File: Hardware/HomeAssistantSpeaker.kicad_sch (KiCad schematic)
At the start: 29 parts, among them J1 USB_C_Receptacle_USB2.0, J2 Speaker, J3 Prog, J4 LED, U1 ESP32-WROOM-32, U2 LM1117-3.3, U3 MAX98357AETE+

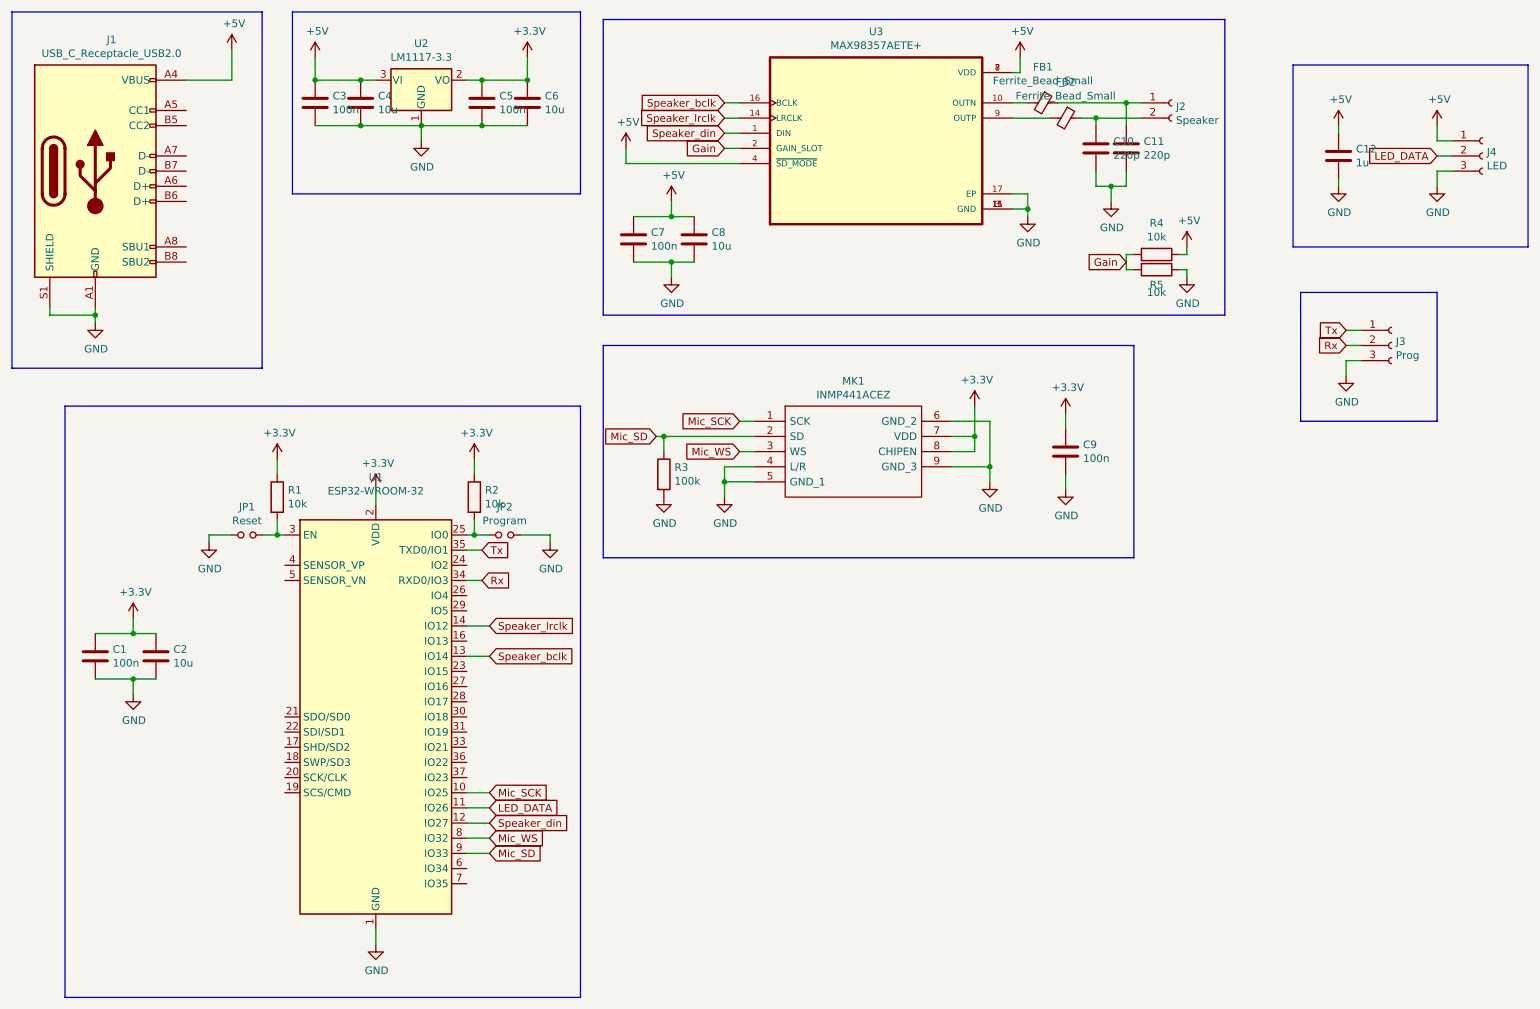
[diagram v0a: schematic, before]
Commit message: Rev B:
* Added missing resitiors for usb c power
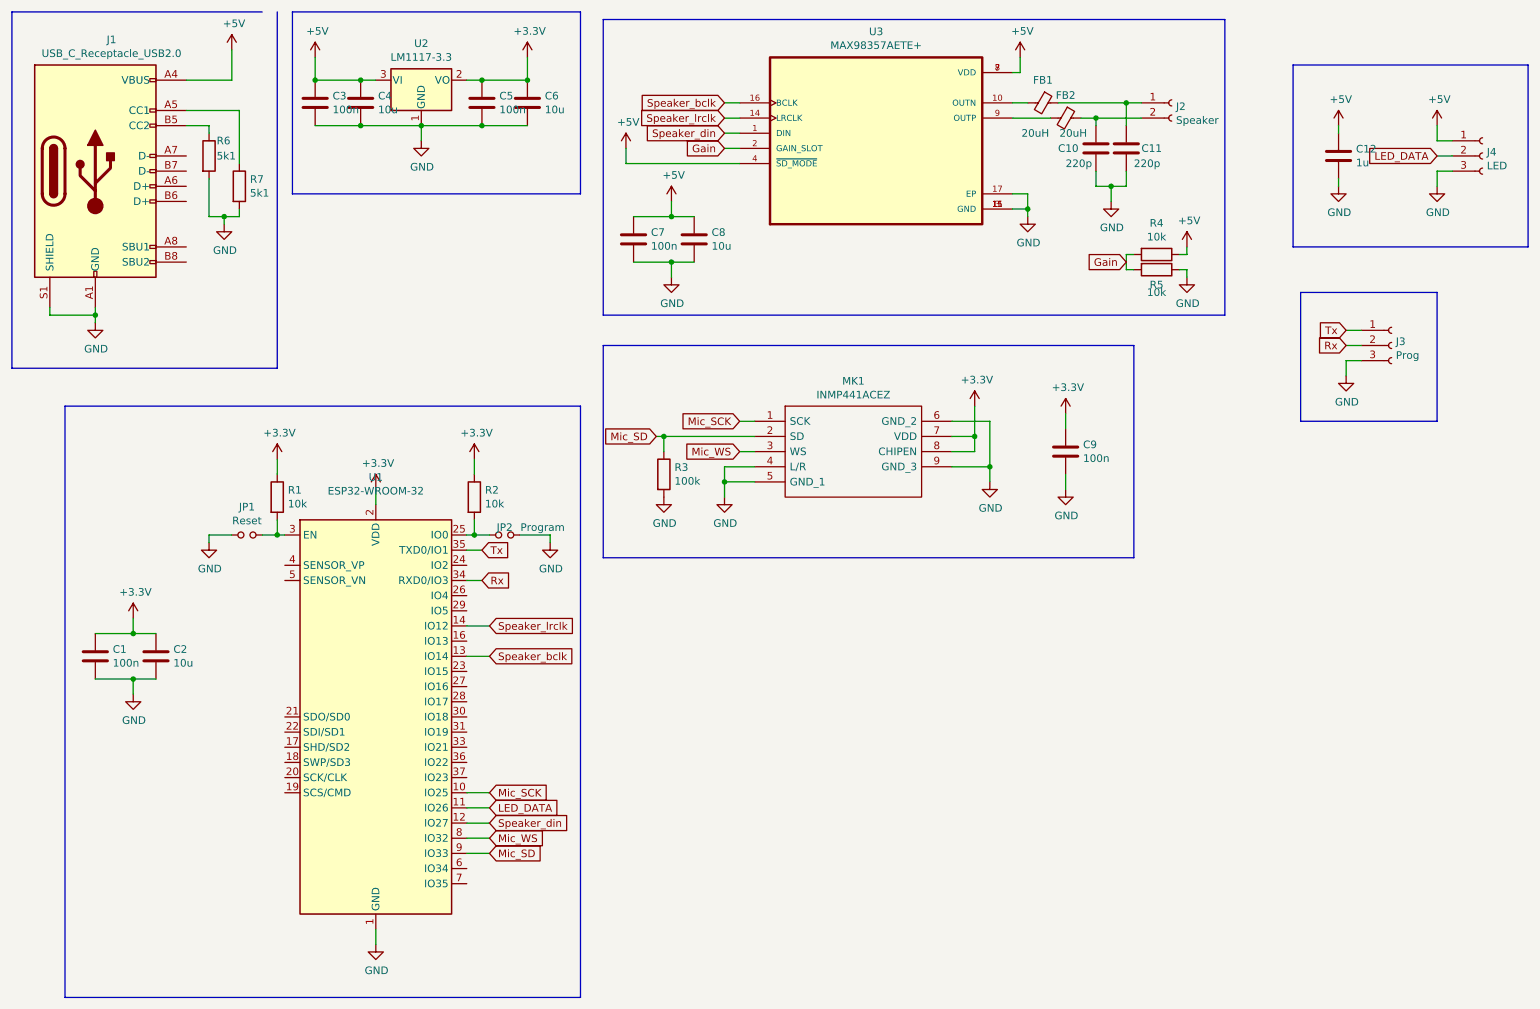
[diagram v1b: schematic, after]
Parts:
- added R6, R7: 5k1, Resistor_SMD:R_0805_2012Metric, symbol Device:R
- FB1, FB2: value Ferrite_Bead_Small -> 20uH
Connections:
- net GND: now also R6.2, R7.2
- net at J1.A5 (CC1): now also R7.1
- net at J1.B5 (CC2): now also R6.1
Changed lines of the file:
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@@
   (title_block
     (title "HomeAssistantSpeaker")
-    (date "2022-11-20")
-    (rev "A")
+    (date "2022-12-29")
+    (rev "B")
     (company "Paweł Warzecha")
   )
@@
   (junction (at 102.87 25.4) (diameter 0) (color 0 0 0 0)
   )
+  (junction (at 52.07 48.26) (diameter 0) (color 0 0 0 0)
+  )
   (junction (at 127 55.88) (diameter 0) (color 0 0 0 0)
   )
@@
     (stroke (width 0) (type default) (color 0 0 0 0))
   )
+  (wire (pts (xy 54.61 30.48) (xy 54.61 39.37))
+    (stroke (width 0) (type default) (color 0 0 0 0))
+  )
   (wire (pts (xy 184.15 46.99) (xy 186.69 46.99))
     (stroke (width 0) (type default) (color 0 0 0 0))
@@
     (stroke (width 0) (type default) (color 0 0 0 0))
   )
+  (wire (pts (xy 49.53 33.02) (xy 49.53 34.29))
+    (stroke (width 0) (type default) (color 0 0 0 0))
+  )
   (wire (pts (xy 96.52 149.86) (xy 92.71 149.86))
     (stroke (width 0) (type default) (color 0 0 0 0))
@@
     (stroke (width 0) (type default) (color 0 0 0 0))
   )
+  (wire (pts (xy 54.61 46.99) (xy 54.61 48.26))
+    (stroke (width 0) (type default) (color 0 0 0 0))
+  )
   (wire (pts (xy 92.71 104.14) (xy 95.25 104.14))
     (stroke (width 0) (type default) (color 0 0 0 0))
@@
     (stroke (width 0) (type default) (color 0 0 0 0))
   )
+  (wire (pts (xy 52.07 48.26) (xy 52.07 49.53))
+    (stroke (width 0) (type default) (color 0 0 0 0))
+  )
   (polyline (pts (xy 204.47 69.85) (xy 115.57 69.85))
     (stroke (width 0) (type default) (color 0 0 0 0))
@@
     (stroke (width 0) (type default) (color 0 0 0 0))
   )
+  (wire (pts (xy 45.72 33.02) (xy 49.53 33.02))
+    (stroke (width 0) (type default) (color 0 0 0 0))
+  )
   (wire (pts (xy 93.98 91.44) (xy 93.98 88.9))
     (stroke (width 0) (type default) (color 0 0 0 0))
@@
     (stroke (width 0) (type default) (color 0 0 0 0))
   )
+  (wire (pts (xy 45.72 30.48) (xy 54.61 30.48))
+    (stroke (width 0) (type default) (color 0 0 0 0))
+  )
   (polyline (pts (xy 255.27 82.55) (xy 232.41 82.55))
     (stroke (width 0) (type default) (color 0 0 0 0))
@@
     (stroke (width 0) (type default) (color 0 0 0 0))
   )
-  (polyline (pts (xy 58.42 73.66) (xy 16.51 73.66))
+  (polyline (pts (xy 60.96 73.66) (xy 16.51 73.66))
+    (stroke (width 0) (type default) (color 0 0 0 0))
+  )
+  (wire (pts (xy 49.53 48.26) (xy 52.07 48.26))
     (stroke (width 0) (type default) (color 0 0 0 0))
   )
@@
     (stroke (width 0) (type default) (color 0 0 0 0))
   )
+  (wire (pts (xy 52.07 48.26) (xy 54.61 48.26))
+    (stroke (width 0) (type default) (color 0 0 0 0))
+  )
   (polyline (pts (xy 63.5 44.45) (xy 63.5 13.97))
     (stroke (width 0) (type default) (color 0 0 0 0))
@@
     (stroke (width 0) (type default) (color 0 0 0 0))
   )
+  (wire (pts (xy 49.53 41.91) (xy 49.53 48.26))
+    (stroke (width 0) (type default) (color 0 0 0 0))
+  )
   (wire (pts (xy 53.34 101.6) (xy 49.53 101.6))
     (stroke (width 0) (type default) (color 0 0 0 0))
@@
     (stroke (width 0) (type default) (color 0 0 0 0))
   )
-  (polyline (pts (xy 58.42 13.97) (xy 58.42 73.66))
+  (polyline (pts (xy 60.96 13.97) (xy 60.96 73.66))
     (stroke (width 0) (type default) (color 0 0 0 0))
   )
@@
   (symbol (lib_id "HomeAssistantSpeaker-rescue:Jumper_NO_Small-Device") (at 99.06 101.6 0) (unit 1)
     (in_bom yes) (on_board yes)
-    (property "Reference" "JP2" (id 0) (at 99.06 96.901 0))
-    (property "Value" "Program" (id 1) (at 99.06 99.2124 0))
+    (property "Reference" "JP2" (id 0) (at 99.06 100.33 0))
+    (property "Value" "Program" (id 1) (at 105.41 100.33 0))
     (property "Footprint" "Jumper:SolderJumper-2_P1.3mm_Open_RoundedPad1.0x1.5mm" (id 2) (at 99.06 101.6 0)
       (effects (font (size 1.27 1.27)) hide)
@@
   (symbol (lib_id "HomeAssistantSpeaker-rescue:Ferrite_Bead_Small-Device") (at 189.23 29.21 270) (unit 1)
     (in_bom yes) (on_board yes)
-    (property "Reference" "FB1" (id 0) (at 189.23 23.1902 90))
-    (property "Value" "Ferrite_Bead_Small" (id 1) (at 189.23 25.5016 90))
+    (property "Reference" "FB1" (id 0) (at 189.23 25.4 90))
+    (property "Value" "20uH" (id 1) (at 187.96 34.29 90))
     (property "Footprint" "Inductor_SMD:L_0805_2012Metric" (id 2) (at 189.23 27.432 90)
       (effects (font (size 1.27 1.27)) hide)
@@
   (symbol (lib_id "HomeAssistantSpeaker-rescue:Ferrite_Bead_Small-Device") (at 193.04 31.75 270) (unit 1)
     (in_bom yes) (on_board yes)
-    (property "Reference" "FB2" (id 0) (at 193.04 25.7302 90))
-    (property "Value" "Ferrite_Bead_Small" (id 1) (at 193.04 28.0416 90))
+    (property "Reference" "FB2" (id 0) (at 193.04 27.94 90))
+    (property "Value" "20uH" (id 1) (at 194.31 34.29 90))
     (property "Footprint" "Inductor_SMD:L_0805_2012Metric" (id 2) (at 193.04 29.972 90)
       (effects (font (size 1.27 1.27)) hide)
@@
   (symbol (lib_id "Device:C") (at 203.2 36.83 0) (unit 1)
     (in_bom yes) (on_board yes)
-    (property "Reference" "C11" (id 0) (at 206.121 35.6616 0)
-      (effects (font (size 1.27 1.27)) (justify left))
-    )
-    (property "Value" "220p" (id 1) (at 206.121 37.973 0)
+    (property "Reference" "C11" (id 0) (at 205.74 36.83 0)
+      (effects (font (size 1.27 1.27)) (justify left))
+    )
+    (property "Value" "220p" (id 1) (at 204.47 39.37 0)
       (effects (font (size 1.27 1.27)) (justify left))
     )
@@
   (symbol (lib_id "Device:C") (at 198.12 36.83 0) (unit 1)
     (in_bom yes) (on_board yes)
-    (property "Reference" "C10" (id 0) (at 201.041 35.6616 0)
-      (effects (font (size 1.27 1.27)) (justify left))
-    )
-    (property "Value" "220p" (id 1) (at 201.041 37.973 0)
+    (property "Reference" "C10" (id 0) (at 191.77 36.83 0)
+      (effects (font (size 1.27 1.27)) (justify left))
+    )
+    (property "Value" "220p" (id 1) (at 193.04 39.37 0)
       (effects (font (size 1.27 1.27)) (justify left))
     )
@@
     (pin "1")
   )
+  (symbol (lib_id "Device:R") (at 54.61 43.18 0) (unit 1)
+    (in_bom yes) (on_board yes)
+    (property "Reference" "R7" (id 0) (at 56.388 42.0116 0)
+      (effects (font (size 1.27 1.27)) (justify left))
+    )
+    (property "Value" "5k1" (id 1) (at 56.388 44.323 0)
+      (effects (font (size 1.27 1.27)) (justify left))
+    )
+    (property "Footprint" "Resistor_SMD:R_0805_2012Metric" (id 2) (at 52.832 43.18 90)
+      (effects (font (size 1.27 1.27)) hide)
+    )
+    (property "Datasheet" "~" (id 3) (at 54.61 43.18 0)
+      (effects (font (size 1.27 1.27)) hide)
+    )
+    (pin "1")
+    (pin "2")
+  )
+  (symbol (lib_id "Device:R") (at 49.53 38.1 0) (unit 1)
+    (in_bom yes) (on_board yes)
+    (property "Reference" "R6" (id 0) (at 50.8 35.56 0)
+      (effects (font (size 1.27 1.27)) (justify left))
+    )
+    (property "Value" "5k1" (id 1) (at 50.8 38.1 0)
+      (effects (font (size 1.27 1.27)) (justify left))
+    )
+    (property "Footprint" "Resistor_SMD:R_0805_2012Metric" (id 2) (at 47.752 38.1 90)
+      (effects (font (size 1.27 1.27)) hide)
+    )
+    (property "Datasheet" "~" (id 3) (at 49.53 38.1 0)
+      (effects (font (size 1.27 1.27)) hide)
+    )
+    (pin "1")
+    (pin "2")
+  )
+  (symbol (lib_id "power:GND") (at 52.07 49.53 0) (unit 1)
+    (in_bom yes) (on_board yes)
+    (property "Reference" "#PWR01" (id 0) (at 52.07 55.88 0)
+      (effects (font (size 1.27 1.27)) hide)
+    )
+    (property "Value" "GND" (id 1) (at 52.197 53.9242 0))
+    (property "Footprint" "" (id 2) (at 52.07 49.53 0)
+      (effects (font (size 1.27 1.27)) hide)
+    )
+    (property "Datasheet" "" (id 3) (at 52.07 49.53 0)
+      (effects (font (size 1.27 1.27)) hide)
+    )
+    (pin "1")
+  )
   (sheet_instances
     (path "/" (page "1"))
   )
   (symbol_instances
+    (path "/c957bf7f-3e92-4741-b985-0817aefda6cb"
+      (reference "#PWR01") (unit 1) (value "GND") (footprint "")
+    )
     (path "/00000000-0000-0000-0000-000062f94a7c"
       (reference "#PWR0101") (unit 1) (value "+5V") (footprint "")
@@
     )
     (path "/00000000-0000-0000-0000-0000637db72b"
-      (reference "FB1") (unit 1) (value "Ferrite_Bead_Small") (footprint "Inductor_SMD:L_0805_2012Metric")
+      (reference "FB1") (unit 1) (value "20uH") (footprint "Inductor_SMD:L_0805_2012Metric")
     )
     (path "/00000000-0000-0000-0000-0000637dc15d"
-      (reference "FB2") (unit 1) (value "Ferrite_Bead_Small") (footprint "Inductor_SMD:L_0805_2012Metric")
+      (reference "FB2") (unit 1) (value "20uH") (footprint "Inductor_SMD:L_0805_2012Metric")
     )
     (path "/00000000-0000-0000-0000-000062f890e9"
@@
       (reference "R5") (unit 1) (value "10k") (footprint "Resistor_SMD:R_0805_2012Metric")
     )
+    (path "/2d4561c2-ecc1-4709-921a-2faf57fc749d"
+      (reference "R6") (unit 1) (value "5k1") (footprint "Resistor_SMD:R_0805_2012Metric")
+    )
+    (path "/038076c1-568f-4cf7-8388-b28feea50ae3"
+      (reference "R7") (unit 1) (value "5k1") (footprint "Resistor_SMD:R_0805_2012Metric")
+    )
     (path "/00000000-0000-0000-0000-00006307ad5f"
